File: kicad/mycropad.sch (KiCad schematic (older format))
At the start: 29 parts, among them SW1 SW_Push, SW2 SW_Push, SW3 SW_Push, SW4 SW_Push, SW5 SW_Push, SW6 SW_Push, SW7 SW_Push, SW8 SW_Push, U1 Pico, U2 SN74AHCT125N

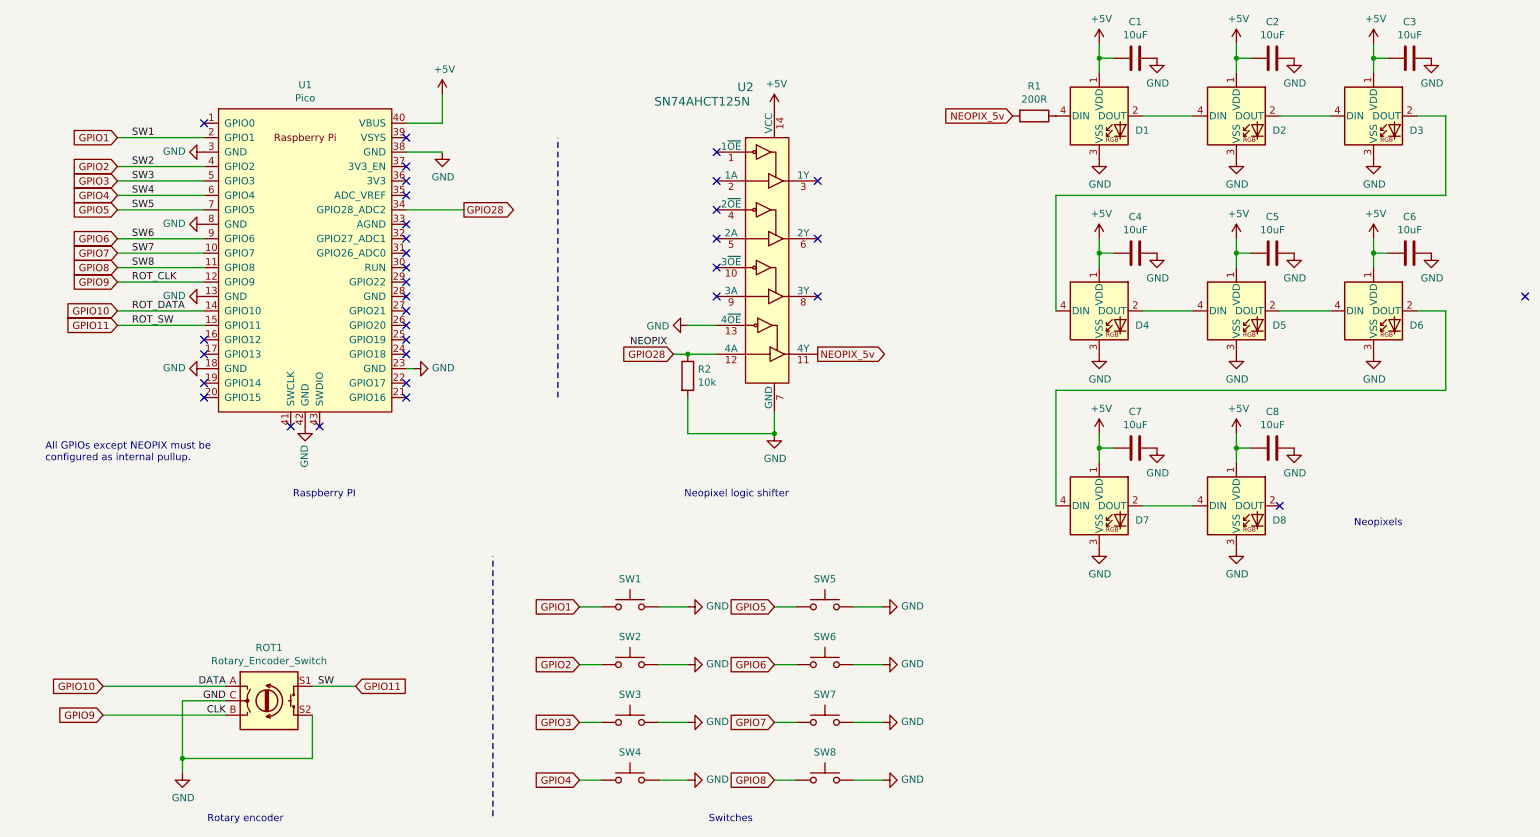
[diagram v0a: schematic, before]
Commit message: Changed board layout, r1 & r2 footprints, added reset button
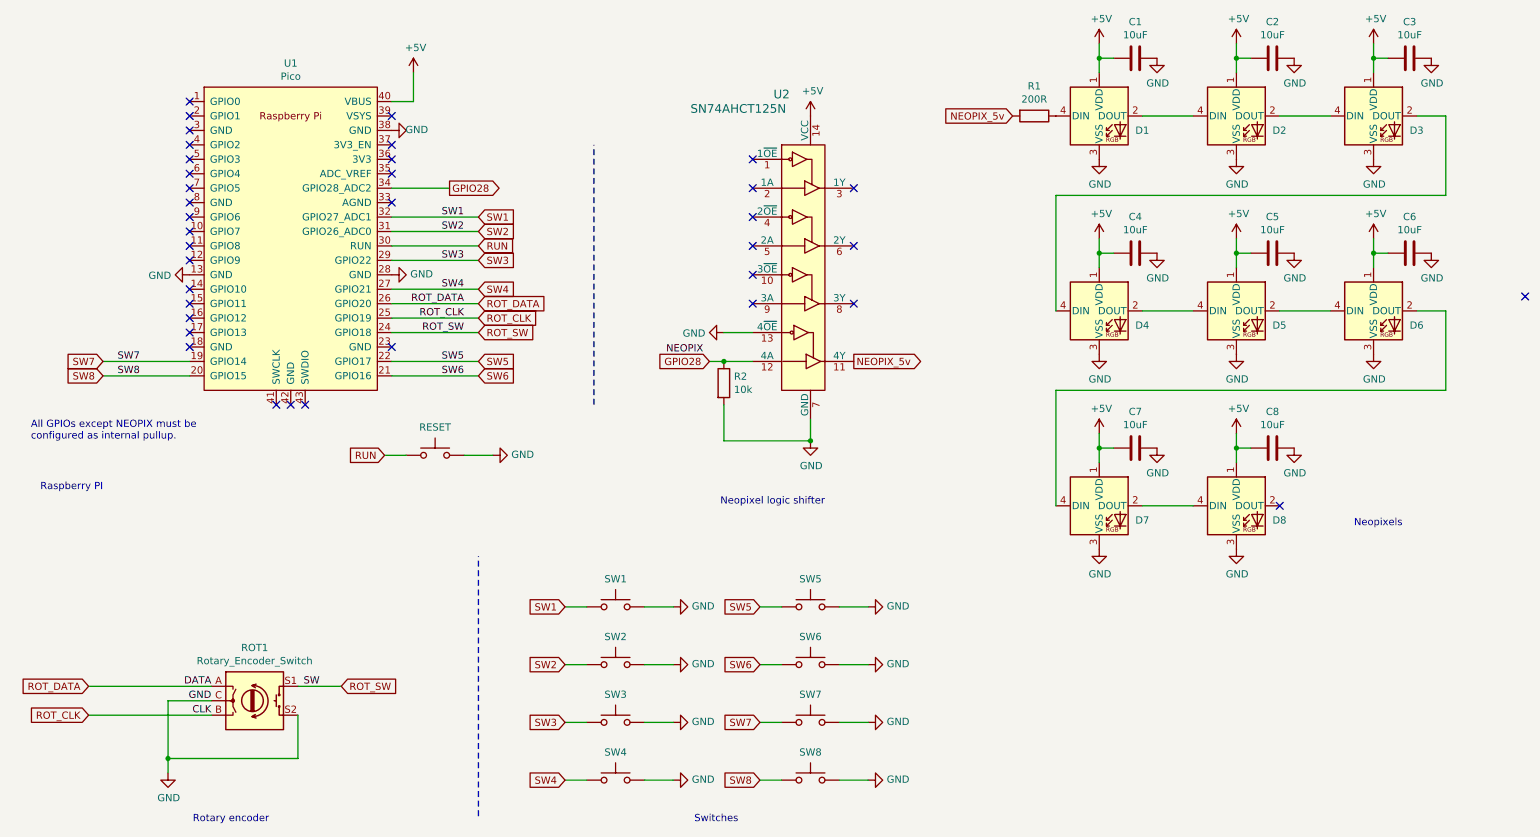
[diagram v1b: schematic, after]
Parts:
- added SW9: RESET, Button_Switch_THT:SW_PUSH_6mm_H4.3mm, symbol Switch:SW_Push
- R1, R2: footprint Resistor_THT:R_Axial_DIN0204_L3.6mm_D1.6mm_P5.08mm_Horizontal -> Resistor_THT:R_Axial_DIN0204_L3.6mm_D1.6mm_P7.62mm_Horizontal
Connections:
- net GND: now also U1.28 (GND), SW9.2; no longer U1.18 (GND), U1.23 (GND), U1.3 (GND), U1.42 (GND), U1.8 (GND)
- net SW7: now reaches U1.19 (GPIO14)
- net SW7: now also SW7.1
- net SW8: now reaches U1.20 (GPIO15)
- net SW8: now also SW8.1
- net SW6: now reaches U1.21 (GPIO16)
- net SW6: now also SW6.1
- net SW5: now reaches U1.22 (GPIO17)
- net SW5: now also SW5.1
- net ROT_SW: now reaches U1.24 (GPIO18)
- net ROT_SW: now also ROT1.S1
- net ROT_CLK: now reaches U1.25 (GPIO19)
- net ROT_CLK: now also ROT1.B
- net ROT_DATA: now reaches U1.26 (GPIO20)
- net ROT_DATA: now also ROT1.A
- net SW4: now reaches U1.27 (GPIO21)
- net SW4: now also SW4.1
- net SW3: now reaches U1.29 (GPIO22)
- net SW3: now also SW3.1
- net RUN: now reaches U1.30 (RUN)
- net RUN: now also SW9.1
- net SW2: now reaches U1.31 (GPIO26_ADC0)
- net SW2: now also SW2.1
- net SW1: now reaches U1.32 (GPIO27_ADC1)
- net SW1: now also SW1.1
- net GPIO1: no longer names the net of U1.2 (GPIO1)
- net GPIO1: no longer SW1.1
- net GPIO10: no longer names the net of U1.14 (GPIO10)
- net GPIO10: no longer ROT1.A
- net GPIO11: no longer names the net of U1.15 (GPIO11)
- net GPIO11: no longer ROT1.S1
- net GPIO2: no longer names the net of U1.4 (GPIO2)
- net GPIO2: no longer SW2.1
- net GPIO3: no longer names the net of U1.5 (GPIO3)
- net GPIO3: no longer SW3.1
- net GPIO4: no longer names the net of U1.6 (GPIO4)
- net GPIO4: no longer SW4.1
- net GPIO5: no longer names the net of U1.7 (GPIO5)
- net GPIO5: no longer SW5.1
- net GPIO6: no longer names the net of U1.9 (GPIO6)
- net GPIO6: no longer SW6.1
- net GPIO7: no longer names the net of U1.10 (GPIO7)
- net GPIO7: no longer SW7.1
- net GPIO8: no longer names the net of U1.11 (GPIO8)
- net GPIO8: no longer SW8.1
- net GPIO9: no longer names the net of U1.12 (GPIO9)
- net GPIO9: no longer ROT1.B
- no-connect marks 34 -> 37
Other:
- moved on the sheet: R2, ROT1, SW1, SW2, SW3, SW4, SW5, SW6, SW7, SW8, U1, U2

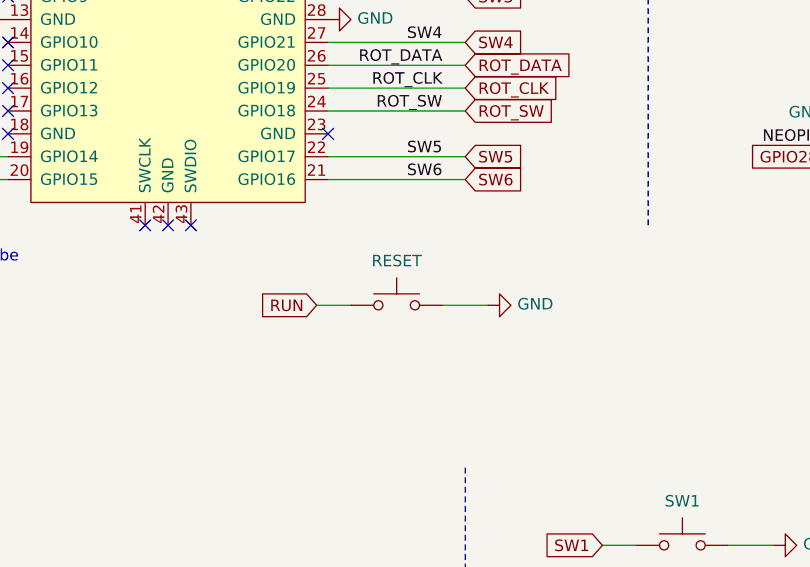
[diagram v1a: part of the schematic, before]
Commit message: Changed holes position
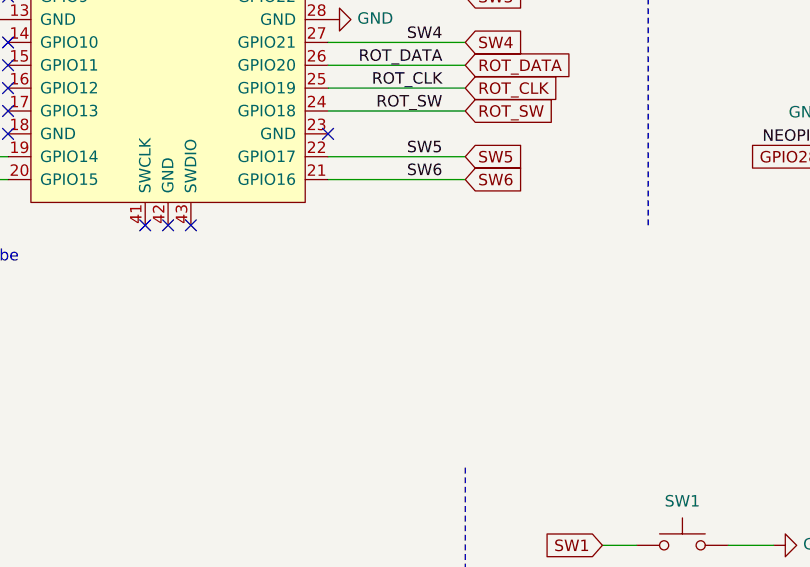
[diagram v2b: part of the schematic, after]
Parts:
- removed SW9: RESET, Button_Switch_THT:SW_PUSH_6mm_H4.3mm, symbol Switch:SW_Push
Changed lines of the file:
@@
-	1    0    0    -1
-$EndComp
-Text GLabel 3050 3750 0    50   Input ~ 0
-RUN
-Wire Wire Line
-	3600 3750 3800 3750
-Wire Wire Line
-	3050 3750 3200 3750
-$Comp
-L power:GND #PWR0132
-U 1 1 61959DE3
-P 3800 3750
-F 0 "#PWR0132" H 3800 3500 50  0001 C CNN
-F 1 "GND" V 3805 3622 50  0000 R CNN
-F 2 "" H 3800 3750 50  0001 C CNN
-F 3 "" H 3800 3750 50  0001 C CNN
-	1    3800 3750
-	0    -1   -1   0
-$EndComp
-$Comp
-L Switch:SW_Push SW9
-U 1 1 61959DE9
-P 3400 3750
-F 0 "SW9" H 3400 3943 50  0001 C CNN
-F 1 "RESET" H 3400 3944 50  0000 C CNN
-F 2 "Button_Switch_THT:SW_PUSH_6mm_H4.3mm" H 3400 3950 50  0001 C CNN
-F 3 "~" H 3400 3950 50  0001 C CNN
-	1    3400 3750
 	1    0    0    -1
 $EndComp
